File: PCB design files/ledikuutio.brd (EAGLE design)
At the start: 120.6 x 83.5 mm, 54 parts, among them IC1 ATMEGA328P, IC3 74HC595D, Q2 MOSFET-NCHANNELSMD, Q3 16mhz, T1 TIP42, T2 TIP42, T3 TIP42, T4 TIP42, T5 TIP42, T6 TIP42, T7 TIP42, T8 TIP42, X1 2516-, X2 5566-20, X3 2516-, X4 2516-, X5 2516-, X6 2510-

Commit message: Updated the designs...
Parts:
- added C18, C19: 100nF, rcl:C0603
- added IC2: ISO7221A, texas:SO-08
- added R11, R12, R13, R14, R15, R16, R17, R18: 1k, rcl:M0805
- F1, F2: value (none) -> 2A; device fuse:GSH15 -> special:FUSE
- R10, R3, R4, R5, R6, R7, R8, R9: device rc-master:R0805 -> rcl:M0805
- R2: device resistor:R0805 -> rcl:M0805
- U$1, U$2, U$3, U$4: value TLC5940TLC5940NT -> TLC5940TLC5940PWP; device elovalo:DIL28 -> elovalo:PWP28
- moved C7 58.9 mm to (22.1, 33.8), turned to 0 degrees
- moved R4 44.7 mm to (90.8, 25.9)
- moved T8 42.9 mm to (91.4, 28.4), turned to 90 degrees
- moved C6 41.9 mm to (16.5, 39.7), turned to 0 degrees
- moved R3 41.7 mm to (84.5, 25.9), turned to 270 degrees
- moved T1 39.2 mm to (85.1, 28.4), turned to 90 degrees
- moved C13 34.6 mm to (99.7, 65.2), turned to 0 degrees
- moved X6 30.7 mm to (101.6, 47.5), turned to 90 degrees
- moved C9 30.5 mm to (99.7, 31.0), turned to 0 degrees
- moved UART 29.2 mm to (3.81, 8.89), turned to 270 degrees
- moved R6 28.9 mm to (90.8, 37.3)
- moved IC3 28.5 mm to (63.3, 34.8)
- moved C10 27.9 mm to (46.2, 39.7), turned to 0 degrees
- moved T7 27.4 mm to (91.4, 39.8), turned to 90 degrees
- moved R5 25.6 mm to (84.5, 37.3)
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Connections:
- removed net DCPRG: IC1.10, U$1.19, U$2.19, U$3.19, U$4.19
- removed net VPRG: IC1.9, U$1.27, U$2.27, U$3.27, U$4.27
- new net GND1: C18.2, IC2.4, UART.1
- new net RXD_FT232R: IC2.3, UART.5
- new net TXD_FT232R: IC2.2, UART.4
- new net VDD: C18.1, IC2.1, UART.3
- net +5V: now also F2.2, IC3.10, U$1.28, U$2.28, U$3.28, U$4.28; no longer F1.1, U$1.21, U$2.21, U$3.21, U$4.21
- net BLANK: now also IC1.14, U$1.2, U$2.2, U$3.2, U$4.2; no longer IC1.11, U$1.23, U$2.23, U$3.23, U$4.23
- net GND: now also C19.2, IC2.5, U$1.1, U$1.26, U$1.6, U$1.THERMAL, U$2.1, U$2.26, U$2.6, U$2.THERMAL, U$3.1, U$3.26, U$3.6, U$3.THERMAL, U$4.1, U$4.26, U$4.6, U$4.THERMAL; no longer U$1.22, U$2.22, U$3.22, U$4.22, UART.1
- net GSCLK/4: now also U$1.25, U$2.25, U$3.25, U$4.25; no longer U$1.18, U$2.18, U$3.18, U$4.18
- net MOSI: now also U$1.5; no longer U$1.26
- net N$1: now also U$1.24, U$2.5; no longer U$1.17, U$2.26
- net N$10: now also R18.2
- net N$11: now also R12.2
- net N$12: now also R13.2
- net N$13: now also R15.2
- net N$14: now also R17.2
- net N$23: now also R13.1
- net N$24: now also R12.1
- net N$25: now also R11.1
- net N$26: now also R14.1
- net N$27: now also R15.1
- net N$28: now also R16.1
- net N$29: now also R17.1
- net N$30: now also R18.1
- net N$32: now also U$1.7; no longer U$1.28
- net N$33: now also U$1.8; no longer U$1.1
- net N$34: now also U$1.9; no longer U$1.2
- net N$35: now also U$1.10; no longer U$1.3
- net N$36: now also U$1.11; no longer U$1.4
- net N$37: now also U$1.12; no longer U$1.5
- net N$38: now also U$1.13; no longer U$1.6
- net N$39: now also U$1.14; no longer U$1.7
- net N$4: now also U$2.24, U$3.5; no longer U$2.17, U$3.26
- net N$40: now also U$1.15; no longer U$1.8
- net N$41: now also U$1.16; no longer U$1.9
- net N$42: now also U$1.17; no longer U$1.10
- net N$43: now also U$1.18; no longer U$1.11
- net N$44: now also U$1.19; no longer U$1.12
- net N$45: now also U$1.20; no longer U$1.13
- net N$46: now also U$1.21; no longer U$1.14
- net N$47: now also U$1.22; no longer U$1.15
- net N$48: now also F2.1; no longer F1.2
- net N$49: now also U$2.7; no longer U$2.28
- net N$5: now also F1.1; no longer F2.2
- net N$50: now also U$2.8; no longer U$2.1
- net N$51: now also U$2.9; no longer U$2.2
- net N$52: now also U$2.10; no longer U$2.3
- net N$53: now also U$2.11; no longer U$2.4
- net N$54: now also U$2.12; no longer U$2.5
- net N$55: now also U$2.13; no longer U$2.6
- net N$56: now also U$2.14; no longer U$2.7
- net N$57: now also U$2.15; no longer U$2.8
- net N$58: now also U$2.16; no longer U$2.9
- net N$59: now also U$2.17; no longer U$2.10
- net N$60: now also U$2.18; no longer U$2.11
- net N$61: now also U$2.19; no longer U$2.12
- net N$62: now also U$2.20; no longer U$2.13
- net N$63: now also U$2.21; no longer U$2.14
- net N$64: now also U$2.22; no longer U$2.15
- net N$65: now also U$3.7; no longer U$3.28
- net N$66: now also U$3.8; no longer U$3.1
- net N$67: now also U$3.9; no longer U$3.2
- net N$68: now also U$3.10; no longer U$3.3
- net N$69: now also U$3.11; no longer U$3.4
- net N$7: now also R11.2
- net N$70: now also U$3.12; no longer U$3.5
- net N$71: now also U$3.13; no longer U$3.6
- net N$72: now also U$3.14; no longer U$3.7
- net N$73: now also U$3.15; no longer U$3.8
- net N$74: now also U$3.16; no longer U$3.9
- net N$75: now also U$3.17; no longer U$3.10
- net N$76: now also U$3.18; no longer U$3.11
- net N$77: now also U$3.19; no longer U$3.12
- net N$78: now also U$3.20; no longer U$3.13
- net N$79: now also U$3.21; no longer U$3.14
- net N$8: now also R14.2
- net N$80: now also U$3.22; no longer U$3.15
- net N$81: now also U$4.7; no longer U$4.28
- net N$82: now also U$4.8; no longer U$4.1
- net N$83: now also U$4.9; no longer U$4.2
- net N$84: now also U$4.10; no longer U$4.3
- net N$85: now also U$4.11; no longer U$4.4
- net N$86: now also U$4.12; no longer U$4.5
- net N$87: now also U$4.13; no longer U$4.6
- net N$88: now also U$4.14; no longer U$4.7
- net N$89: now also U$4.15; no longer U$4.8
- net N$9: now also R16.2
- net N$90: now also U$4.16; no longer U$4.9
- net N$91: now also U$4.17; no longer U$4.10
- net N$92: now also U$4.18; no longer U$4.11
- net N$93: now also U$4.19; no longer U$4.12
- net N$94: now also U$4.20; no longer U$4.13
- net N$95: now also U$4.21; no longer U$4.14
- net N$96: now also U$4.22; no longer U$4.15
- net N$97: now also U$3.24, U$4.5; no longer U$3.17, U$4.26
- net PS_ON: now also IC1.1; no longer IC1.2
- net RXD: now also IC2.6; no longer UART.4
- net SCLK: now also U$1.4, U$2.4, U$3.4, U$4.4; no longer U$1.25, U$2.25, U$3.25, U$4.25
- net TLC_SOUT: now also U$4.24; no longer U$4.17
- net TXD: now also IC2.7; no longer UART.5
- net VCC: now also C19.1, F1.2, IC2.8; no longer F2.1, IC3.10, UART.3
- net XLAT: now also U$1.3, U$2.3, U$3.3, U$4.3; no longer U$1.24, U$2.24, U$3.24, U$4.24
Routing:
- net VCC: track 0.00 -> 108.3 mm, vias 0 -> 5
- net +5V: track 0.00 -> 80.4 mm
- net XLAT: track 0.00 -> 58.8 mm
- net SCLK: track 0.00 -> 58.5 mm
- net BLANK: track 0.00 -> 57.0 mm
- net GSCLK/4: track 0.00 -> 55.3 mm, vias 0 -> 4
- net PS_ON: track 0.00 -> 50.6 mm, vias 0 -> 1
- net N$47: track 0.00 -> 35.0 mm
- net N$82: track 0.00 -> 32.5 mm
- net N$81: track 0.00 -> 31.4 mm
- net N$45: track 0.00 -> 30.5 mm
- net N$46: track 0.00 -> 29.5 mm
- net N$84: track 0.00 -> 28.7 mm
- net N$80: track 0.00 -> 27.6 mm
- net N$83: track 0.00 -> 27.5 mm
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- added copper zone on layer 16, net B_CUT_ISOLATION
- added copper zone on layer 1, net GND1
- added copper zone on layer 16, net GND1
- added copper zone on layer 1, net T_CUT_ISOLATION
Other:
- board size 120.6 x 83.5 mm -> 128.2 x 69.5 mm

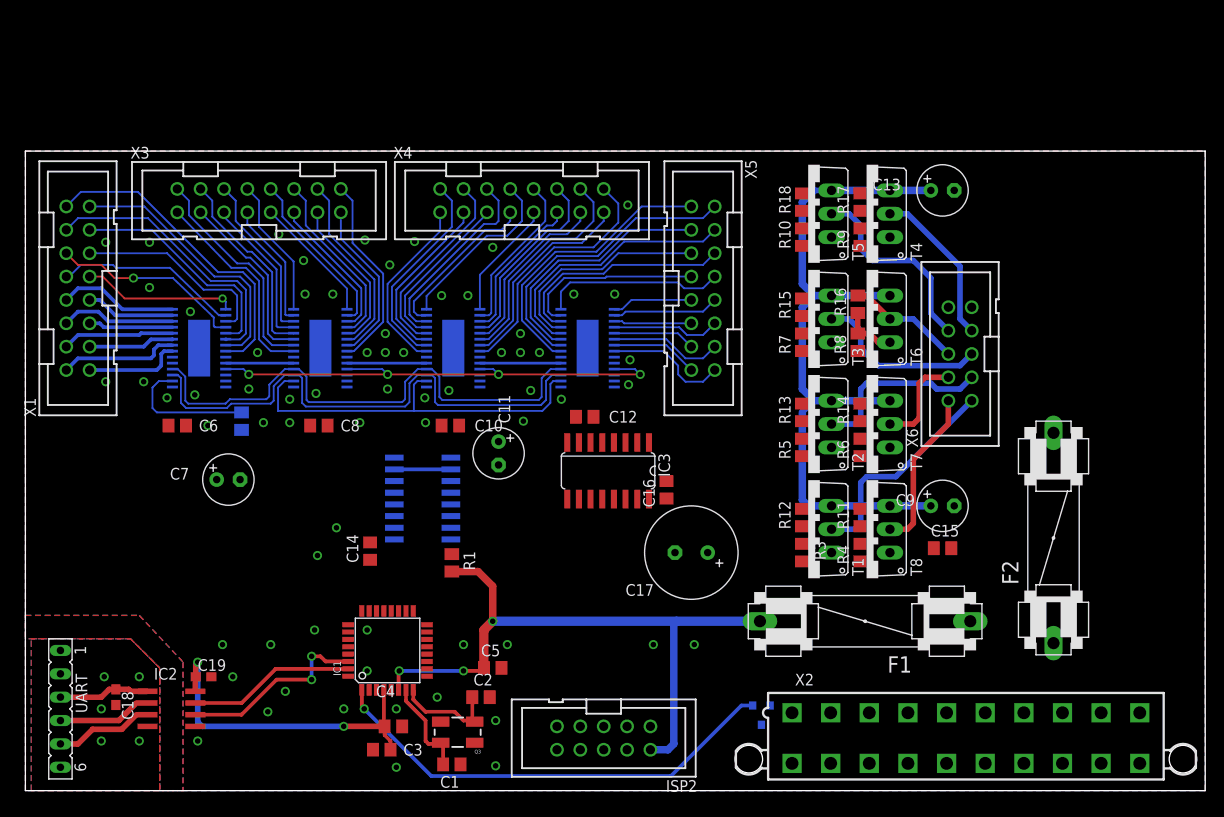
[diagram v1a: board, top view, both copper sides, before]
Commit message: Signal area in PCB almost ready.
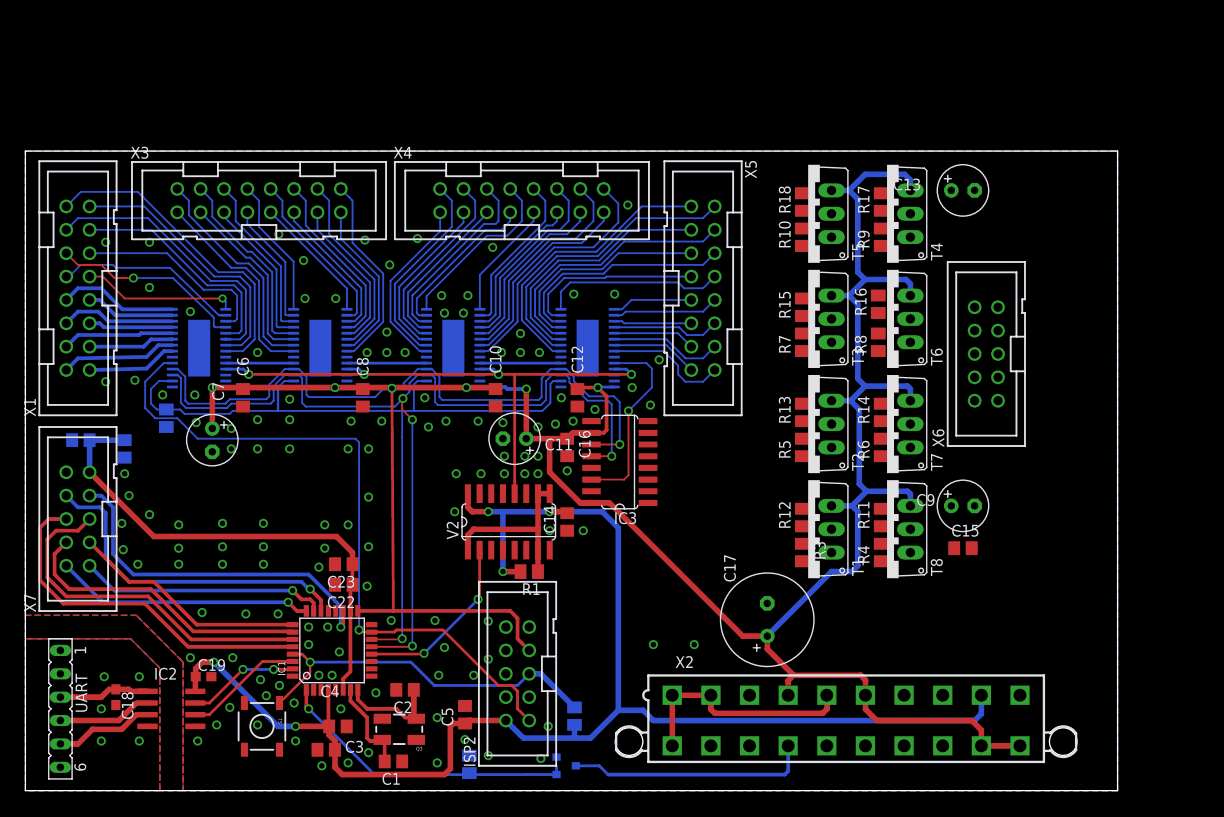
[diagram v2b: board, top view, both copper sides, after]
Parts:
- removed F1, F2: 2A, special:FUSE
- added C20, C22: 10nF, rcl:C0805
- added C21, C23: 100nF, rcl:C0805
- added R19, R20: 10k, rcl:M0805
- added S1: RESET, SparkFun:TACTILE_SWITCH_SMD
- added X7: ANALOG IO, con-3m:PAK100/2500-10
- moved Q2 22.0 mm to (58.7, 2.70), turned to 90 degrees
- moved C14 21.7 mm to (58.9, 29.2)
- moved X2 13.2 mm to (89.2, 7.62)
- moved C16 11.7 mm to (58.9, 37.3), turned to 270 degrees
- moved ISP2 11.7 mm to (53.5, 12.7), turned to 90 degrees
- moved C17 11.0 mm to (80.6, 18.6), turned to 90 degrees
- moved V2 9.70 mm to (52.5, 29.2), flipped to the top, turned to 0 degrees
- moved R1 8.47 mm to (54.8, 23.8), turned to 180 degrees
- moved C2 8.29 mm to (41.3, 11.0), turned to 180 degrees
- moved R2 8.18 mm to (15.3, 40.5)
- moved C6 7.75 mm to (23.7, 42.7), turned to 90 degrees
- moved Q3 6.36 mm to (40.6, 6.67)
- moved C1 6.36 mm to (40.0, 3.17)
- moved C4 6.03 mm to (34.0, 6.99)
- moved C3 6.03 mm to (32.7, 4.45)
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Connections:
- removed net AGND: IC1.21
- removed net AVCC: IC1.18
- removed net N$48: C17.+, F2.1, X2.19, X2.20, X2.4, X2.6
- removed net N$5: F1.1, X2.9
- new net ADC0: IC1.23, X7.1
- new net ADC1: IC1.24, X7.2
- new net ADC2: IC1.25, X7.3
- new net ADC3: IC1.26, X7.4
- new net ADC4: IC1.27, X7.5
- new net ADC5: IC1.28, X7.6
- new net ADC6: IC1.19, X7.7
- new net ADC7: IC1.22, X7.8
- net +5V: now also C17.+, X2.19, X2.20, X2.4, X2.6; no longer F2.2
- net GND: now also C20.2, C21.2, C22.2, C23.2, IC1.21, R19.2, S1.3, X7.10
- net PS_ON: now also R19.1
- net RESET: now also R20.1, S1.1
- net VCC: now also C20.1, C21.1, C22.1, C23.1, IC1.18, R20.2, X2.9, X7.9; no longer F1.2
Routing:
- net +5V: track 80.4 -> 238.0 mm, vias 0 -> 5
- net VCC: track 108.3 -> 215.1 mm
- net MOSI: track 0.00 -> 75.7 mm, vias 0 -> 1
- net SCLK: track 58.5 -> 118.5 mm, vias 0 -> 2
- net XLAT: track 58.8 -> 105.0 mm, vias 0 -> 4
- net RESET: track 0.00 -> 39.9 mm, vias 0 -> 1
- net ADC5: track 0.00 -> 39.4 mm
- net ADC6: track 0.00 -> 39.4 mm, vias 0 -> 1
- net ADC4: track 0.00 -> 39.1 mm
- net ADC7: track 0.00 -> 36.5 mm, vias 0 -> 1
- net ADC3: track 0.00 -> 32.5 mm
- net BLANK: track 57.0 -> 89.0 mm, vias 0 -> 1
- net ADC1: track 0.00 -> 28.1 mm, vias 0 -> 1
- net ADC0: track 0.00 -> 26.9 mm, vias 0 -> 1
- net N$31: track 0.00 -> 26.4 mm
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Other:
- board size 128.2 x 69.5 mm -> 118.7 x 69.5 mm

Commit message: Make first fully routed PCB file.
The first fully routed PCB file, fixed some supply issues also.
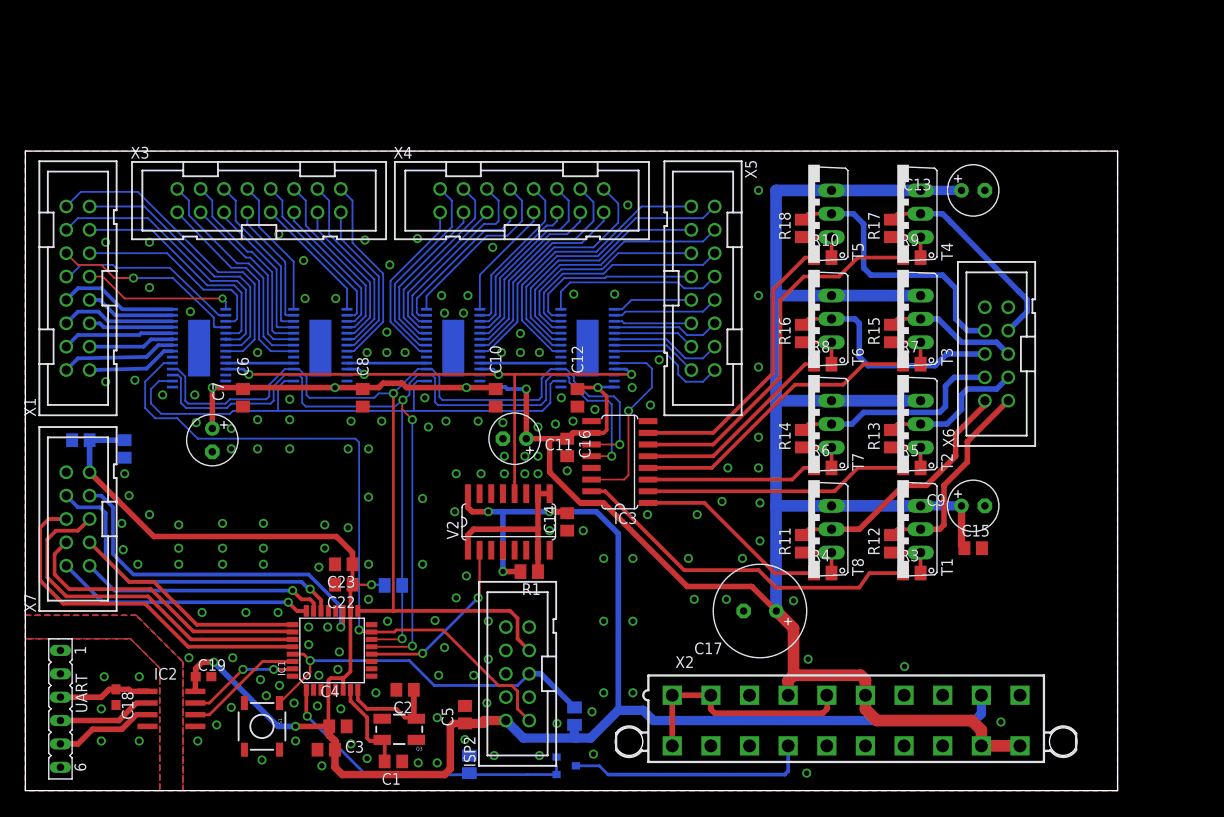
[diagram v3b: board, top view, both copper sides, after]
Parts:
- moved R2 30.7 mm to (40.0, 22.3), turned to 0 degrees
- moved R7 12.1 mm to (96.4, 46.4), turned to 0 degrees
- moved R3 12.1 mm to (96.4, 23.7), turned to 0 degrees
- moved R5 12.1 mm to (96.4, 35.1), turned to 0 degrees
- moved R12 10.1 mm to (94.1, 26.8)
- moved R13 10.1 mm to (94.1, 38.3)
- moved R15 10.1 mm to (94.1, 49.7)
- moved T1 9.68 mm to (94.8, 28.4)
- moved T2 9.68 mm to (94.8, 39.8)
- moved T3 9.68 mm to (94.8, 51.3)
- moved R11 9.04 mm to (84.5, 26.8)
- moved R14 9.04 mm to (84.5, 38.3)
- moved R16 8.84 mm to (84.5, 49.7)
- moved T6 8.57 mm to (85.1, 51.3)
- moved T7 8.57 mm to (85.1, 39.8)
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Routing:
- net N$21: track 0.00 -> 41.1 mm
- net N$15: track 0.00 -> 39.0 mm
- net N$19: track 0.00 -> 32.4 mm
- net N$22: track 0.00 -> 31.2 mm
- net N$10: track 0.00 -> 30.1 mm
- net N$17: track 0.00 -> 28.8 mm
- net +5V: track 238.0 -> 266.7 mm
- net N$7: track 0.00 -> 27.6 mm
- net N$9: track 0.00 -> 24.9 mm
- net N$8: track 0.00 -> 23.5 mm
- net N$14: track 0.00 -> 23.1 mm
- net N$11: track 0.00 -> 22.6 mm
- net N$20: track 0.00 -> 22.2 mm
- net N$16: track 0.00 -> 21.2 mm
- net N$18: track 0.00 -> 18.6 mm
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
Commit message: Add up to date schematics.pdf and minor changes to the chematic and layout.
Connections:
- net GND: now also S1.2; no longer S1.3
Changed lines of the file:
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@@
 <via x="25.24125" y="37.1475" extent="1-16" drill="0.6" diameter="0.9"/>
 <via x="37.30625" y="37.1475" extent="1-16" drill="0.6" diameter="0.8"/>
-<contactref element="S1" pad="3"/>
+<contactref element="S1" pad="2"/>
 <via x="22.38375" y="39.37" extent="1-16" drill="0.6" diameter="0.8"/>
 <via x="32.86125" y="17.78" extent="1-16" drill="0.6" diameter="0.8"/>
